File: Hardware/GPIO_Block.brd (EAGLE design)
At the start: 30.5 x 71.1 mm, 22 parts, among them U1 TXB0108, U2 EDISON_CONNECTOR_FULLMOUNTING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, U3 EDISON_CONNECTOR_FULLHEADER, U4 TXB0108

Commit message: t/bRestrict between connector pads. (v10)
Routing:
- net GND: track 0.00 -> 27.5 mm
- net VSYS: track 47.1 -> 52.4 mm
- net 1.8V: track 69.5 -> 70.8 mm
- net 3.3V: track 60.3 -> 61.5 mm, vias 1 -> 3
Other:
- board text added: "v10"
- board text removed: "v02"

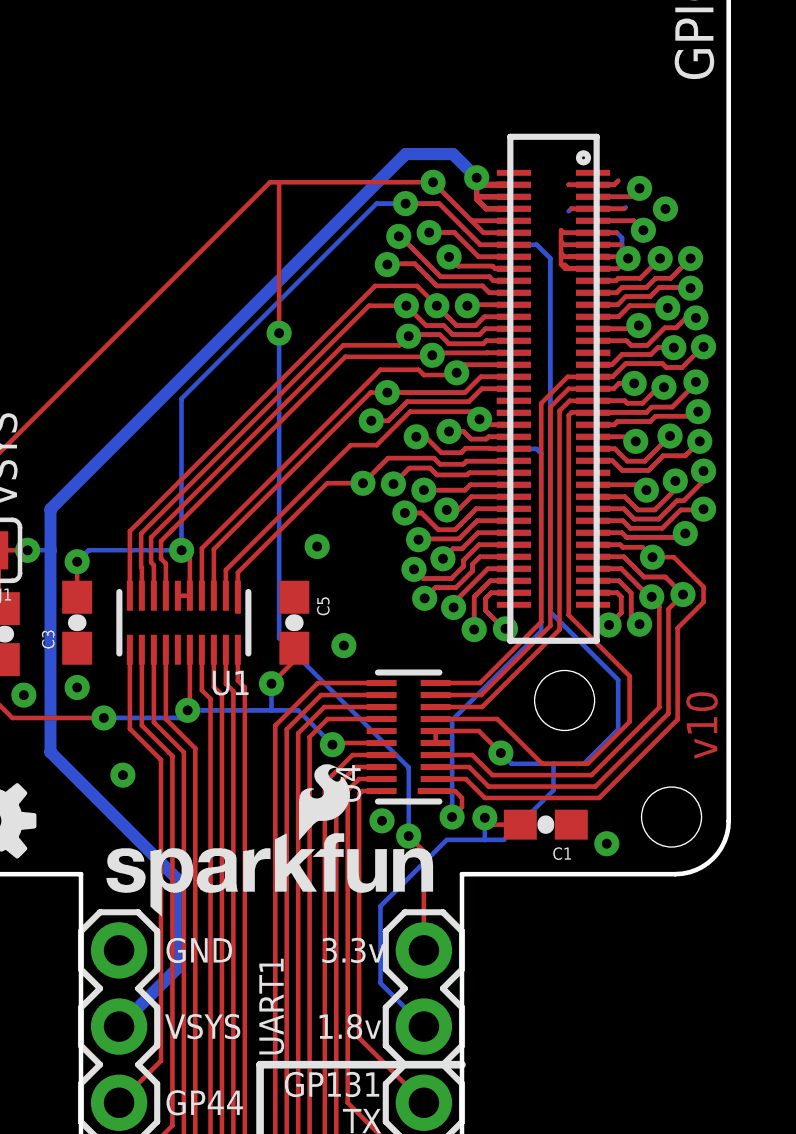
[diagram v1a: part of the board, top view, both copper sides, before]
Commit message: Re-routing 3.3v line
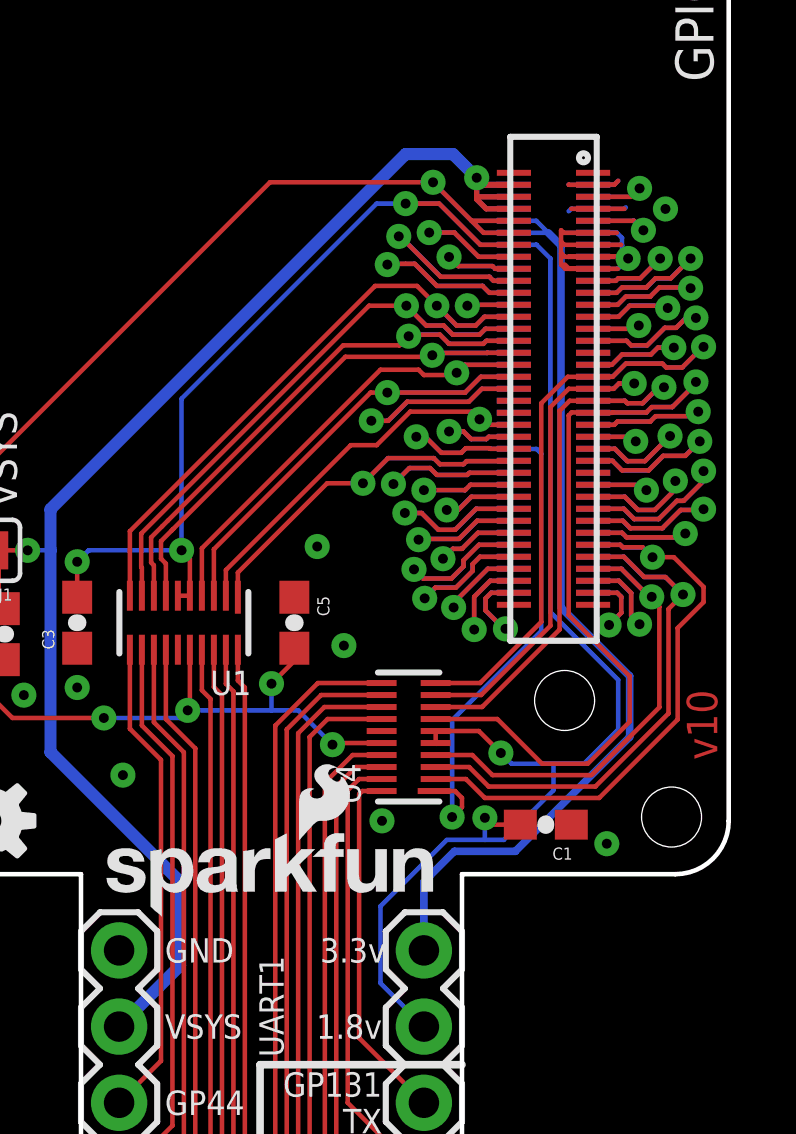
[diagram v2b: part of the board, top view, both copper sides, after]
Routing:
- net 3.3V: track 61.5 -> 65.4 mm, vias 3 -> 1
- net GND: track 27.5 -> 26.8 mm
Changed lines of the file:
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@@
 <setting verticaltext="up"/>
 </settings>
-<grid distance="0.01" unitdist="inch" unit="inch" style="lines" multiple="1" display="yes" altdistance="0.005" altunitdist="inch" altunit="inch"/>
+<grid distance="0.05" unitdist="inch" unit="inch" style="lines" multiple="1" display="yes" altdistance="0.005" altunitdist="inch" altunit="inch"/>
 <layers>
 <layer number="1" name="Top" color="4" fill="1" visible="yes" active="yes"/>
-<layer number="2" name="Route2" color="1" fill="3" visible="yes" active="yes"/>
+<layer number="2" name="Route2" color="1" fill="3" visible="no" active="yes"/>
 <layer number="15" name="Route15" color="4" fill="6" visible="no" active="yes"/>
 <layer number="16" name="Bottom" color="1" fill="1" visible="yes" active="yes"/>
@@
 <wire x1="25.96" y1="22.18" x2="27.006" y2="22.18" width="0.1524" layer="1"/>
 <wire x1="25.96" y1="20.18" x2="26.784" y2="20.18" width="0.1524" layer="16"/>
-<wire x1="26.784" y1="20.18" x2="27.1272" y2="20.5232" width="0.1524" layer="16"/>
+<wire x1="26.784" y1="20.18" x2="27.051" y2="20.447" width="0.1524" layer="16"/>
+<wire x1="27.051" y1="20.447" x2="27.1272" y2="20.5232" width="0.1524" layer="16"/>
 <wire x1="25.96" y1="21.38" x2="26.753" y2="21.38" width="0.1524" layer="16"/>
 <wire x1="26.753" y1="21.38" x2="26.924" y2="21.209" width="0.1524" layer="16"/>
@@
 <wire x1="25.96" y1="20.5798" x2="27.1722" y2="20.5798" width="0.1524" layer="1"/>
 <wire x1="27.1722" y1="20.5798" x2="27.178" y2="20.574" width="0.1524" layer="1"/>
-<wire x1="25.96" y1="20.5798" x2="27.1722" y2="20.5798" width="0.1524" layer="16"/>
+<wire x1="26.9182" y1="20.5798" x2="27.1722" y2="20.5798" width="0.1524" layer="16"/>
 <wire x1="25.96" y1="20.58" x2="25.914" y2="20.58" width="0.1524" layer="16"/>
 <wire x1="25.914" y1="20.58" x2="25.908" y2="20.574" width="0.1524" layer="16"/>
 <wire x1="25.908" y1="20.574" x2="25.908" y2="20.5798" width="0.1524" layer="16"/>
-<wire x1="25.96" y1="20.58" x2="25.152" y2="20.58" width="0.1524" layer="16"/>
-<wire x1="25.152" y1="20.58" x2="25.146" y2="20.574" width="0.1524" layer="16"/>
-<wire x1="25.96" y1="21.3798" x2="24.9752" y2="21.3798" width="0.1524" layer="16"/>
 <wire x1="25.96" y1="20.9798" x2="24.9942" y2="20.9798" width="0.1524" layer="1"/>
-<wire x1="25.96" y1="20.9798" x2="24.9942" y2="20.9798" width="0.1524" layer="16"/>
-<wire x1="25.96" y1="20.1798" x2="25.0322" y2="20.1798" width="0.1524" layer="16"/>
+<wire x1="25.96" y1="20.5798" x2="27.0452" y2="20.5798" width="0.1524" layer="1"/>
+<wire x1="27.0452" y1="20.5798" x2="27.051" y2="20.574" width="0.1524" layer="1"/>
+<wire x1="24.9752" y1="21.3798" x2="26.7528" y2="21.3798" width="0.1524" layer="16"/>
+<wire x1="26.7528" y1="21.3798" x2="26.753" y2="21.38" width="0.1524" layer="16"/>
+<wire x1="25.96" y1="20.5798" x2="26.9182" y2="20.5798" width="0.1524" layer="16"/>
+<wire x1="26.9182" y1="20.5798" x2="27.051" y2="20.447" width="0.1524" layer="16"/>
+<wire x1="25.96" y1="20.5798" x2="25.96" y2="20.58" width="0.1524" layer="16"/>
 </signal>
 <signal name="VSYS">
@@
 <wire x1="4.5212" y1="10.795" x2="4.5212" y2="9.0542" width="0.1524" layer="1"/>
 <wire x1="4.5212" y1="9.0542" x2="4.318" y2="8.851" width="0.1524" layer="1"/>
-<wire x1="15.1892" y1="23.0632" x2="15.494" y2="23.0632" width="0.1524" layer="1"/>
 <via x="20.6248" y="23.0632" extent="1-16" drill="0.3302"/>
-<wire x1="15.494" y1="23.0632" x2="20.6248" y2="23.0632" width="0.1524" layer="1"/>
+<wire x1="15.1892" y1="23.0632" x2="20.6248" y2="23.0632" width="0.1524" layer="1"/>
 <wire x1="20.6248" y1="23.0632" x2="21.908" y2="21.78" width="0.1524" layer="16"/>
 <wire x1="22.3082" y1="21.3798" x2="21.908" y2="21.78" width="0.1524" layer="1"/>
@@
 <wire x1="23.32" y1="21.3798" x2="23.32" y2="21.38" width="0.1524" layer="16"/>
 <wire x1="23.32" y1="21.78" x2="23.32" y2="21.7798" width="0.1524" layer="1"/>
-<wire x1="20.32" y1="-2.54" x2="20.32" y2="0.762" width="0.1524" layer="1"/>
-<wire x1="20.32" y1="0.762" x2="19.812" y2="1.27" width="0.1524" layer="1"/>
-<via x="19.812" y="1.27" extent="1-16" drill="0.3302"/>
-<wire x1="19.812" y1="1.27" x2="19.812" y2="3.556" width="0.1524" layer="16"/>
-<wire x1="19.812" y1="3.556" x2="15.494" y2="7.874" width="0.1524" layer="16"/>
-<wire x1="15.494" y1="7.874" x2="15.494" y2="18.034" width="0.1524" layer="16"/>
-<via x="15.494" y="18.034" extent="1-16" drill="0.3302"/>
-<wire x1="15.494" y1="18.034" x2="15.494" y2="23.0632" width="0.1524" layer="1"/>
+<wire x1="20.32" y1="-2.54" x2="20.32" y2="-0.254" width="0.254" layer="16"/>
+<wire x1="20.32" y1="-0.254" x2="21.336" y2="0.762" width="0.254" layer="16"/>
+<wire x1="21.336" y1="0.762" x2="23.368" y2="0.762" width="0.254" layer="16"/>
+<wire x1="23.368" y1="0.762" x2="27.178" y2="4.572" width="0.254" layer="16"/>
+<wire x1="27.178" y1="4.572" x2="27.178" y2="6.604" width="0.254" layer="16"/>
+<wire x1="27.178" y1="6.604" x2="24.892" y2="8.89" width="0.254" layer="16"/>
+<wire x1="24.892" y1="8.89" x2="24.892" y2="20.955" width="0.254" layer="16"/>
+<wire x1="24.067" y1="21.78" x2="23.32" y2="21.78" width="0.1524" layer="16"/>
+<wire x1="24.4672" y1="21.3798" x2="23.32" y2="21.3798" width="0.1524" layer="16"/>
+<wire x1="24.892" y1="20.955" x2="24.4672" y2="21.3798" width="0.254" layer="16"/>
+<wire x1="24.4672" y1="21.3798" x2="24.067" y2="21.78" width="0.1524" layer="16"/>
 </signal>
 <signal name="GP183_PWM3">

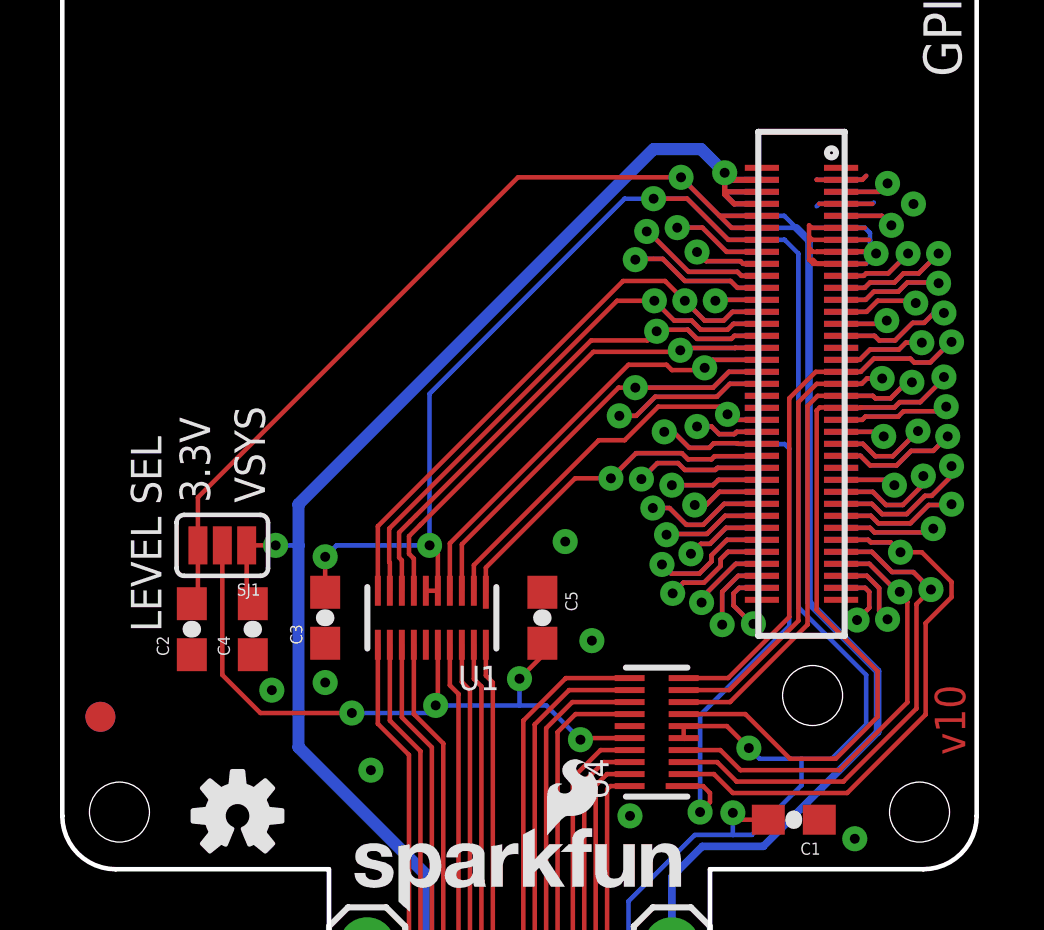
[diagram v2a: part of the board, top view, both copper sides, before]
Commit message: Adding silk to bottom. Slight trace re-routes.
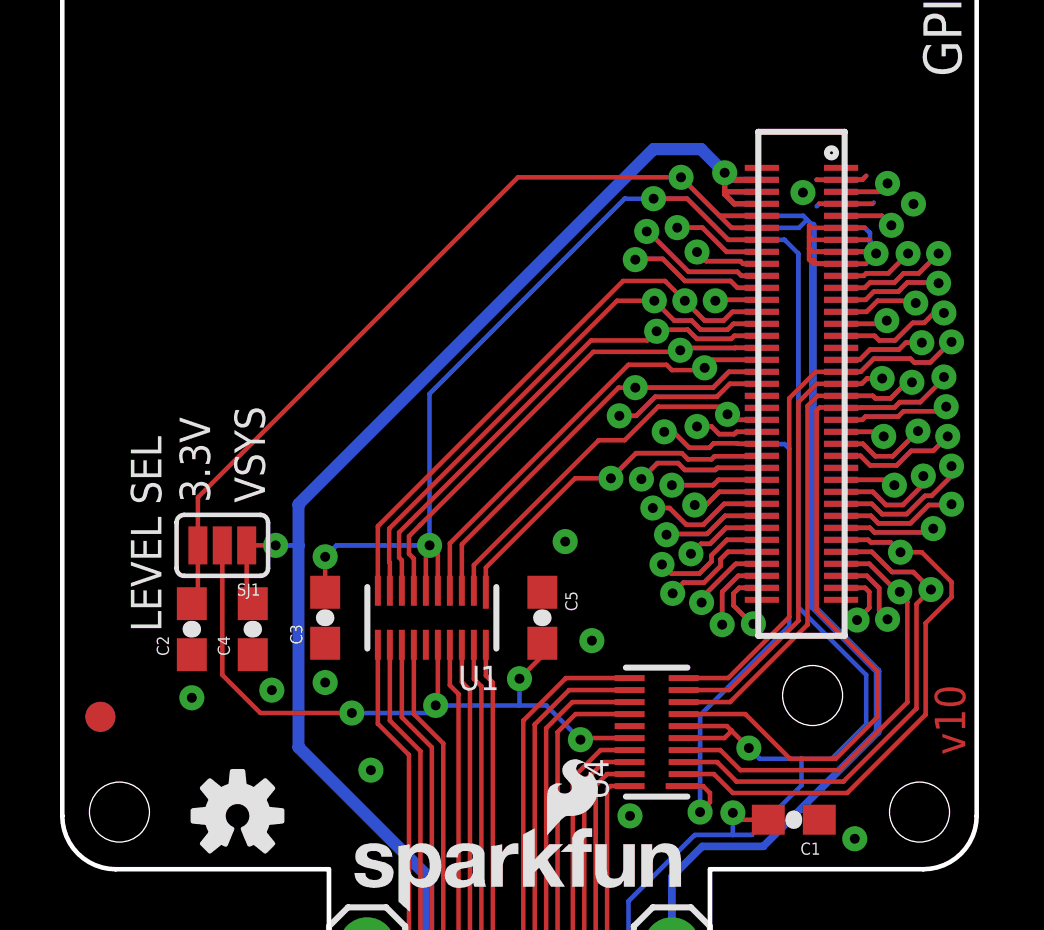
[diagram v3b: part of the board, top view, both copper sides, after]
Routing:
- net 1.8V: track 70.8 -> 73.2 mm
- net 3.3V: track 65.4 -> 66.2 mm
- net GND: track 26.8 -> 26.2 mm, vias 9 -> 11
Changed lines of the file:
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@@
 <rectangle x1="22.098" y1="26.162" x2="30.48" y2="44.45" layer="42" rot="R180"/>
 <rectangle x1="22.098" y1="26.162" x2="30.48" y2="44.45" layer="41" rot="R180"/>
-<text x="29.21" y="6.35" size="1.016" layer="22" font="vector" ratio="15" rot="MR90" align="center">4xM2.0</text>
+<text x="29.21" y="6.223" size="1.016" layer="22" font="vector" ratio="15" rot="SMR270" align="center">4xM2.0</text>
 <text x="30.099" y="3.81" size="1.016" layer="1" font="vector" ratio="15" rot="R90">v10</text>
 <text x="11.684" y="-7.62" size="0.8128" layer="21" font="vector" ratio="15" align="center-left">GP44</text>
@@
 <text x="29.972" y="36.83" size="1.27" layer="22" font="vector" ratio="15" rot="SMR270">GPIO Block</text>
 <text x="25.4" y="-5.08" size="1.778" layer="51">NOTE: Units are in Inches</text>
-<text x="4.9276" y="12.2174" size="1.016" layer="21" ratio="15" rot="R90">3.3V</text>
-<text x="5.7404" y="12.2174" size="1.016" layer="21" ratio="15" rot="R90" align="top-left">VSYS</text>
-<text x="3.302" y="11.176" size="1.016" layer="21" ratio="15" rot="R90" align="bottom-center">LEVEL SEL</text>
+<text x="4.9276" y="12.2174" size="1.016" layer="21" font="vector" ratio="15" rot="R90">3.3V</text>
+<text x="5.7404" y="12.2174" size="1.016" layer="21" font="vector" ratio="15" rot="R90" align="top-left">VSYS</text>
+<text x="3.302" y="11.176" size="1.016" layer="21" font="vector" ratio="15" rot="R90" align="bottom-center">LEVEL SEL</text>
+<text x="11.303" y="-7.62" size="0.8128" layer="22" font="vector" ratio="15" rot="MR0" align="center-right">GP44</text>
+<text x="11.303" y="-10.16" size="0.8128" layer="22" font="vector" ratio="15" rot="MR0" align="center-right">GP45</text>
+<text x="11.303" y="-12.573" size="0.8128" layer="22" font="vector" ratio="15" rot="MR0" align="center-right">GP46</text>
+<text x="11.303" y="-15.24" size="0.8128" layer="22" font="vector" ratio="15" rot="MR0" align="center-right">GP47</text>
+<text x="11.303" y="-17.78" size="0.8128" layer="22" font="vector" ratio="15" rot="MR0" align="center-right">GP48</text>
+<text x="11.303" y="-20.32" size="0.8128" layer="22" font="vector" ratio="15" rot="MR0" align="center-right">GP49</text>
+<text x="11.303" y="-22.86" size="0.8128" layer="22" font="vector" ratio="15" rot="MR0" align="center-right">GP15</text>
+<text x="11.303" y="-25.4" size="0.8128" layer="22" font="vector" ratio="15" rot="MR0" align="center-right">GP14</text>
+<text x="11.303" y="-5.08" size="0.8128" layer="22" font="vector" ratio="15" rot="MR0" align="center-right">VSYS</text>
+<text x="11.303" y="-2.54" size="0.8128" layer="22" font="vector" ratio="15" rot="MR0" align="center-right">GND</text>
+<text x="19.05" y="-2.54" size="0.8128" layer="22" font="vector" ratio="15" rot="MR180" align="center-right">3.3v</text>
+<text x="19.05" y="-5.08" size="0.8128" layer="22" font="vector" ratio="15" rot="MR180" align="center-right">1.8v</text>
+<text x="19.05" y="-7.62" size="0.8128" layer="22" font="vector" ratio="15" rot="MR0" align="center-left">GP131
+TX</text>
+<text x="19.05" y="-10.16" size="0.8128" layer="22" font="vector" ratio="15" rot="MR0" align="center-left">GP130
+RX</text>
+<text x="19.05" y="-12.7" size="0.8128" layer="22" font="vector" ratio="15" rot="MR0" align="center-left">GP129
+RTS</text>
+<text x="19.05" y="-15.24" size="0.8128" layer="22" font="vector" ratio="15" rot="MR0" align="center-left">GP128
+CTS</text>
+<text x="19.05" y="-17.78" size="0.8128" layer="22" font="vector" ratio="15" rot="MR0" align="center-left">GP183
+PWM3</text>
+<text x="19.05" y="-20.32" size="0.8128" layer="22" font="vector" ratio="15" rot="MR0" align="center-left">GP182
+PWM2</text>
+<text x="19.05" y="-22.86" size="0.8128" layer="22" font="vector" ratio="15" rot="MR0" align="center-left">GP12
+PWM0</text>
+<text x="19.05" y="-25.4" size="0.8128" layer="22" font="vector" ratio="15" rot="MR0" align="center-left">GP13
+PWM1</text>
+<text x="15.24" y="-6.096" size="0.8128" layer="22" font="vector" ratio="15" rot="MR90" align="center-left">UART1</text>
+<wire x1="21.59" y1="-16.51" x2="14.859" y2="-16.51" width="0.254" layer="22"/>
+<wire x1="14.859" y1="-6.35" x2="14.859" y2="-16.51" width="0.254" layer="22"/>
+<wire x1="14.859" y1="-6.35" x2="21.59" y2="-6.35" width="0.254" layer="22"/>
 </plain>
 <attributes>
@@
 <wire x1="25.96" y1="20.5798" x2="27.0452" y2="20.5798" width="0.1524" layer="1"/>
 <wire x1="27.0452" y1="20.5798" x2="27.051" y2="20.574" width="0.1524" layer="1"/>
-<wire x1="24.9752" y1="21.3798" x2="26.7528" y2="21.3798" width="0.1524" layer="16"/>
+<wire x1="25.6102" y1="21.3798" x2="26.7528" y2="21.3798" width="0.1524" layer="16"/>
 <wire x1="26.7528" y1="21.3798" x2="26.753" y2="21.38" width="0.1524" layer="16"/>
 <wire x1="25.96" y1="20.5798" x2="26.9182" y2="20.5798" width="0.1524" layer="16"/>
 <wire x1="26.9182" y1="20.5798" x2="27.051" y2="20.447" width="0.1524" layer="16"/>
 <wire x1="25.96" y1="20.5798" x2="25.96" y2="20.58" width="0.1524" layer="16"/>
+<via x="24.6888" y="22.5552" extent="1-16" drill="0.3302"/>
+<via x="4.318" y="5.715" extent="1-16" drill="0.3302"/>
 </signal>
 <signal name="VSYS">
@@
 <wire x1="23.368" y1="0.762" x2="27.178" y2="4.572" width="0.254" layer="16"/>
 <wire x1="27.178" y1="4.572" x2="27.178" y2="6.604" width="0.254" layer="16"/>
-<wire x1="27.178" y1="6.604" x2="24.892" y2="8.89" width="0.254" layer="16"/>
-<wire x1="24.892" y1="8.89" x2="24.892" y2="20.955" width="0.254" layer="16"/>
-<wire x1="24.067" y1="21.78" x2="23.32" y2="21.78" width="0.1524" layer="16"/>
-<wire x1="24.4672" y1="21.3798" x2="23.32" y2="21.3798" width="0.1524" layer="16"/>
-<wire x1="24.892" y1="20.955" x2="24.4672" y2="21.3798" width="0.254" layer="16"/>
-<wire x1="24.4672" y1="21.3798" x2="24.067" y2="21.78" width="0.1524" layer="16"/>
+<wire x1="27.178" y1="6.604" x2="25.019" y2="8.763" width="0.254" layer="16"/>
+<wire x1="25.019" y1="8.763" x2="25.019" y2="21.336" width="0.254" layer="16"/>
+<wire x1="24.702" y1="21.78" x2="23.32" y2="21.78" width="0.1524" layer="16"/>
+<wire x1="24.702" y1="21.78" x2="25.019" y2="21.463" width="0.1524" layer="16"/>
+<wire x1="25.019" y1="21.463" x2="25.019" y2="21.336" width="0.254" layer="16"/>
+<wire x1="23.32" y1="21.3798" x2="24.5548" y2="21.3798" width="0.1524" layer="16"/>
+<wire x1="24.5548" y1="21.3798" x2="24.765" y2="21.59" width="0.1524" layer="16"/>
 </signal>
 <signal name="GP183_PWM3">
@@
 <contactref element="U4" pad="5"/>
 <contactref element="U4" pad="6"/>
-<wire x1="20.712" y1="4.372" x2="20.712" y2="4.772" width="0.1524" layer="1"/>
 <contactref element="U1" pad="5"/>
 <contactref element="U1" pad="6"/>
@@
 <wire x1="23.241" y1="3.683" x2="22.8854" y2="4.0386" width="0.1524" layer="16"/>
 <via x="22.8854" y="4.0386" extent="1-16" drill="0.3302"/>
-<wire x1="22.8854" y1="4.0386" x2="22.152" y2="4.772" width="0.1524" layer="1"/>
+<wire x1="22.8854" y1="4.0386" x2="22.3" y2="4.624" width="0.1524" layer="1"/>
 <wire x1="22.152" y1="4.772" x2="20.712" y2="4.772" width="0.1524" layer="1"/>
 <wire x1="18.8722" y1="-3.6322" x2="18.8722" y2="-1.0668" width="0.1524" layer="16"/>
@@
 <wire x1="22.987" y1="1.143" x2="24.638" y2="2.794" width="0.1524" layer="16"/>
 <wire x1="24.638" y1="2.794" x2="24.638" y2="3.683" width="0.1524" layer="16"/>
-<wire x1="12.119" y1="9.282" x2="12.519" y2="9.282" width="0.1524" layer="1"/>
 <via x="12.2428" y="10.795" extent="1-16" drill="0.3302"/>
 <wire x1="12.2428" y1="10.795" x2="12.519" y2="10.5188" width="0.1524" layer="1"/>
 <wire x1="12.519" y1="10.5188" x2="12.519" y2="9.282" width="0.1524" layer="1"/>
-<wire x1="20.7406" y1="4.3434" x2="20.712" y2="4.372" width="0.1524" layer="1"/>
 <wire x1="12.2428" y1="10.795" x2="12.2428" y2="15.8496" width="0.1524" layer="16"/>
 <contactref element="C1" pad="2"/>
@@
 <wire x1="22.2002" y1="20.9798" x2="23.32" y2="20.9798" width="0.1524" layer="1"/>
 <wire x1="18.7452" y1="22.352" x2="19.7104" y2="22.352" width="0.1524" layer="16"/>
+<wire x1="12.119" y1="9.282" x2="12.119" y2="10.6712" width="0.1524" layer="1"/>
+<wire x1="12.119" y1="10.6712" x2="12.2428" y2="10.795" width="0.1524" layer="1"/>
+<wire x1="22.152" y1="4.772" x2="22.3" y2="4.624" width="0.1524" layer="1"/>
+<wire x1="22.3" y1="4.624" x2="22.3" y2="4.6" width="0.1524" layer="1"/>
+<wire x1="20.712" y1="4.372" x2="22.072" y2="4.372" width="0.1524" layer="1"/>
+<wire x1="22.072" y1="4.372" x2="22.3" y2="4.6" width="0.1524" layer="1"/>
 </signal>
 <signal name="FW_RCVR">
